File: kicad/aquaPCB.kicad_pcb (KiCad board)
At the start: 2 copper layers, 100 x 100 mm, 149 parts, among them J1 12V IN, J11 SSR G17, J12 SSR G22, J13 SSR G23, J14 SSR G27, J15 IN1, J16 IN2, J17 IN3, J18 IN4, J19 1-Wire 1, J2 Raspberry Pi, J22 I2C 1, J23 I2C 2, J24 Display, J25 pH probe, J26 Module, J27 AIN3, J4 OUT G18, J5 OUT G19, J6 OUT G12, J7 OUT G13, J8 OUT G16, J9 OUT G26, Q1 AOD4184A, Q10 AOD4185, Q2 AOD4184A, Q3 AOD4184A, Q4 AOD4184A, Q5 AOD4184A, Q6 AOD4184A, U1 TPS54360B, U2 AMS1117-3.3, U3 74HCT244D, U4 ULN2803A, U5 ADS1115IDGSR, U6 TLV9062IDR

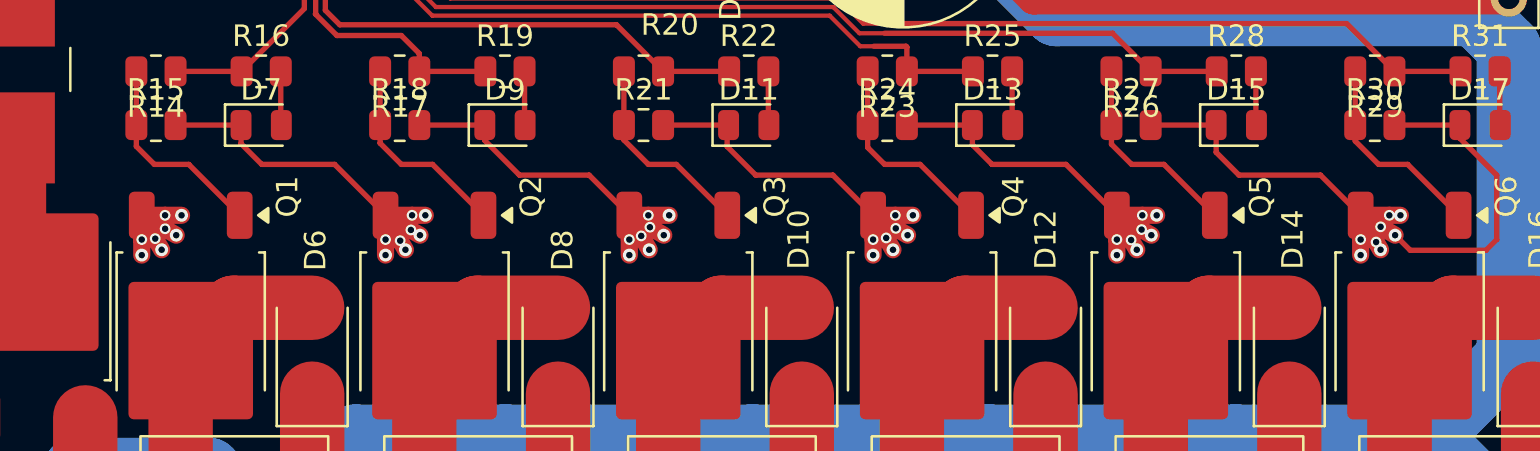
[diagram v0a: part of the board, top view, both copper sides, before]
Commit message: kicad: regular 2x3 source-via blocks with F.Cu GND areas at Q1..Q6
Replaces the 8 crowded vias per MOSFET source (6 hole_to_hole violations)
with 6 vias 0.3/0.6 on a 1 mm grid next to the source pad, joined to the
pad by a small solid F.Cu GND zone (SRC_Qn, priority 2).

Co-Authored-By: Claude Opus 5.5 <noreply@anthropic.com>
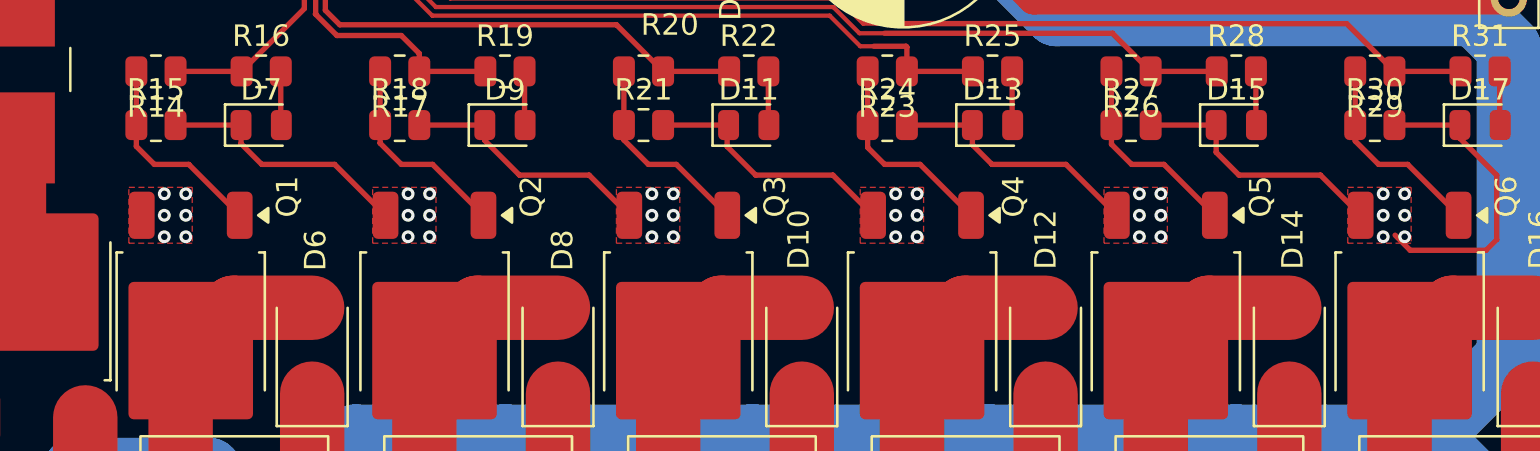
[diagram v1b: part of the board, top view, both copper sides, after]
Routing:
- net GND: track 434.6 -> 390.2 mm, vias 68 -> 56
- added copper zone on F.Cu, net GND

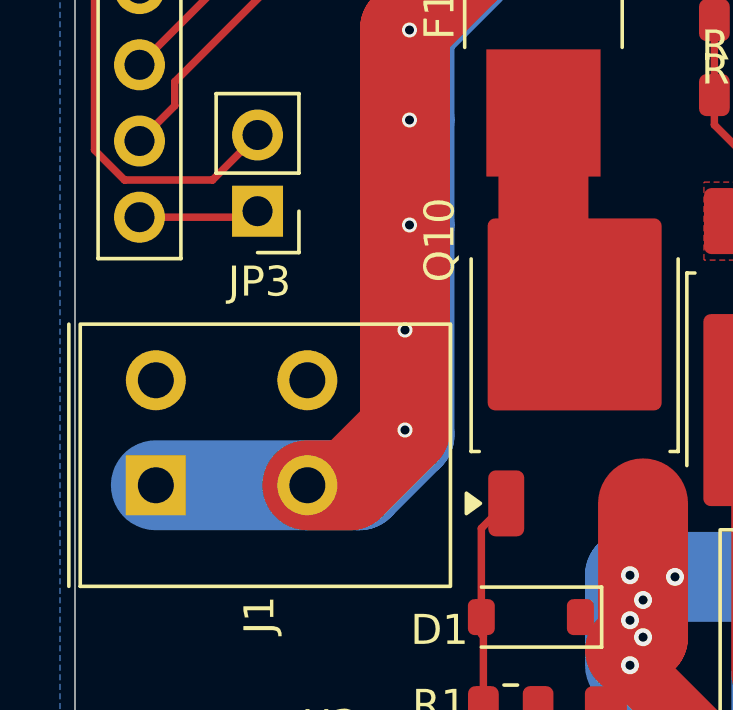
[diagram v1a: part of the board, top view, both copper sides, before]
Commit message: kicad: swap J1 pins (pin 1 = GND), remove floating GND islands
J1 GND now sits on the lower pole, so the ground plane leaves the input
terminal directly east towards Q1..Q6 instead of being boxed in by the
VIN_RAW B.Cu feed. VIN_RAW now starts at the upper pole (3 mm on both
layers as before). Schematic: J1 rotated 180 deg instead of mirrored, wiring
unchanged. GND B.Cu zone island removal set to "always" (removes the
floating 1.05 mm2 island next to J1).

Co-Authored-By: Claude Opus 5.5 <noreply@anthropic.com>
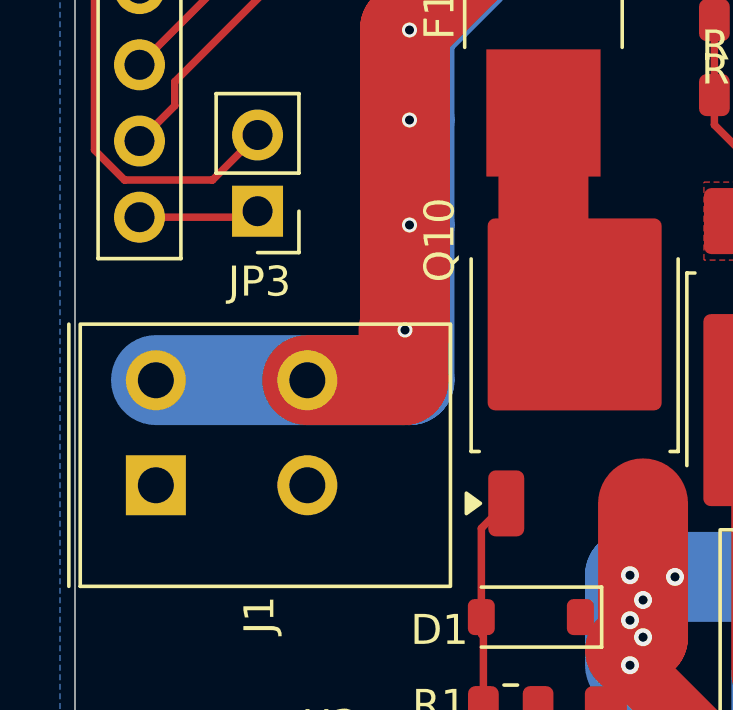
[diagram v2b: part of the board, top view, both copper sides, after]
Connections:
- J1 pad 1: /Power supply/VIN_RAW -> GND
- J1 pad 2: GND -> /Power supply/VIN_RAW
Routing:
- net /Power supply/VIN_RAW: track 49.0 -> 44.0 mm, vias 6 -> 5
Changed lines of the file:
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@@
 			(layers "*.Cu" "*.Mask")
 			(remove_unused_layers no)
-			(net "/Power supply/VIN_RAW")
+			(net "GND")
 			(pinfunction "Pin_1_1")
 			(pintype "passive")
@@
 			(layers "*.Cu" "*.Mask")
 			(remove_unused_layers no)
-			(net "/Power supply/VIN_RAW")
+			(net "GND")
 			(pinfunction "Pin_1_1")
 			(pintype "passive")
@@
 			(layers "*.Cu" "*.Mask")
 			(remove_unused_layers no)
-			(net "GND")
+			(net "/Power supply/VIN_RAW")
 			(pinfunction "Pin_2_2")
 			(pintype "passive")
@@
 			(layers "*.Cu" "*.Mask")
 			(remove_unused_layers no)
-			(net "GND")
+			(net "/Power supply/VIN_RAW")
 			(pinfunction "Pin_2_2")
 			(pintype "passive")
@@
 	)
 	(segment
+		(start 89.8 118.17)
+		(end 89.8 116.5)
+		(width 3)
+		(layer "F.Cu")
+		(net "/Power supply/VIN_RAW")
+	)
+	(segment
 		(start 89.85 116.5)
 		(end 89.85 106.455)
@@
 	)
 	(segment
-		(start 88.009213 121.675)
-		(end 89.85 119.834213)
-		(width 3)
-		(layer "F.Cu")
-		(net "/Power supply/VIN_RAW")
-	)
-	(segment
-		(start 89.85 119.834213)
-		(end 89.85 116.5)
-		(width 3)
-		(layer "F.Cu")
-		(net "/Power supply/VIN_RAW")
-	)
-	(segment
-		(start 86.595 121.675)
-		(end 88.009213 121.675)
+		(start 86.59 118.17)
+		(end 89.8 118.17)
 		(width 3)
 		(layer "F.Cu")
@@
 	)
 	(via
-		(at 89.85 119.834213)
-		(size 0.5)
-		(drill 0.3)
-		(layers "F.Cu" "B.Cu")
-		(net "/Power supply/VIN_RAW")
-	)
-	(via
 		(at 89.85 116.5)
 		(size 0.5)
@@
 	)
 	(segment
-		(start 88.325 121.675)
-		(end 90 120)
-		(width 3)
-		(layer "B.Cu")
-		(net "/Power supply/VIN_RAW")
-	)
-	(segment
 		(start 90 106.5)
 		(end 92 104.5)
@@
 	)
 	(segment
-		(start 81.545 121.675)
-		(end 86.595 121.675)
+		(start 81.55 118.17)
+		(end 86.59 118.17)
 		(width 3)
 		(layer "B.Cu")
@@
 	)
 	(segment
-		(start 90 120)
-		(end 90 113)
+		(start 90 109.5)
+		(end 90 106.5)
 		(width 3)
 		(layer "B.Cu")
@@
 	)
 	(segment
-		(start 90 109.5)
-		(end 90 106.5)
+		(start 86.59 118.17)
+		(end 90 118.17)
 		(width 3)
 		(layer "B.Cu")
@@
 	)
 	(segment
-		(start 86.595 121.675)
-		(end 88.325 121.675)
+		(start 90 118.17)
+		(end 90 113)
 		(width 3)
 		(layer "B.Cu")

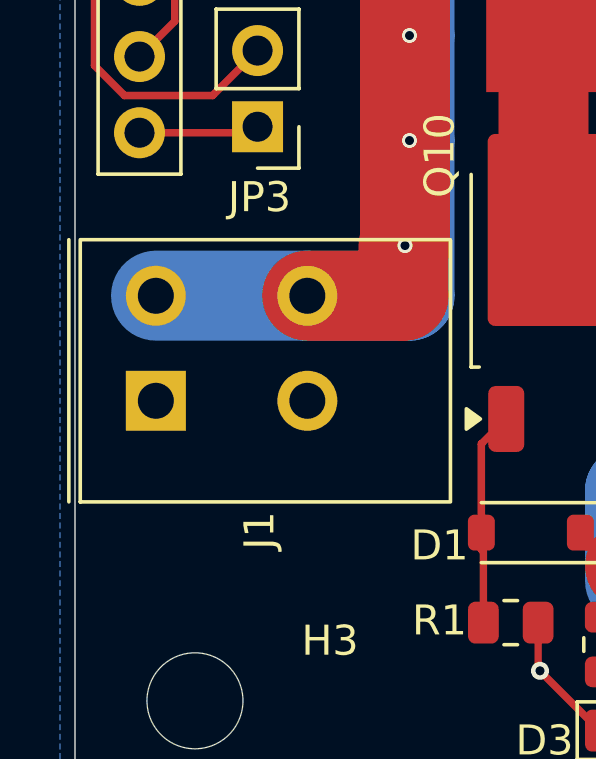
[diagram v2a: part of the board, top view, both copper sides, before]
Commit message: kicad: J1 polarity silk (+12V/GND), connector values match aquaPi port names
Terminal values now use the IoRegistry port names (PWM 0/1, GPIO n,
DS1820, ADC #1 in n) instead of the old "OUT G18"-style labels, several of
which were stale after the 74HCT244 reorder. Values stay on F.Fab; only the
J1 polarity marks are added to the silkscreen.

Co-Authored-By: Claude Opus 5.5 <noreply@anthropic.com>
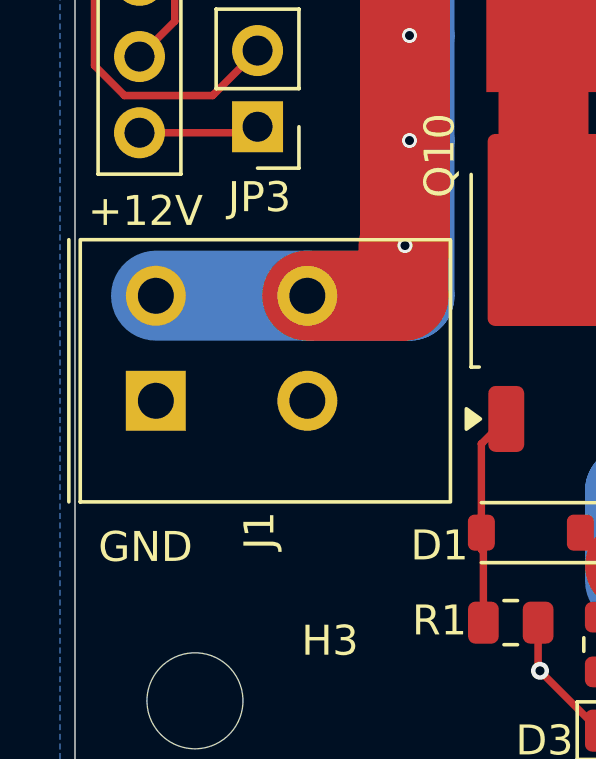
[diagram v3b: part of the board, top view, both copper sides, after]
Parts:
- J11: value SSR G17 -> GPIO 17
- J12: value SSR G22 -> GPIO 22
- J13: value SSR G23 -> GPIO 23
- J14: value SSR G27 -> GPIO 27
- J15: value IN1 -> GPIO 5
- J16: value IN2 -> GPIO 6
- J17: value IN3 -> GPIO 20
- J18: value IN4 -> GPIO 21
- J19: value 1-Wire 1 -> DS1820
- J25: value pH probe -> ADC #1 in 0
- J26: value Module -> ADC #1 in 2
- J27: value AIN3 -> ADC #1 in 3
- J4: value OUT G18 -> PWM 0
- J5: value OUT G19 -> GPIO 12
- J6: value OUT G12 -> GPIO 13
- J7: value OUT G13 -> PWM 1
- J8: value OUT G16 -> GPIO 16
- J9: value OUT G26 -> GPIO 26
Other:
- board text added: "+12V"
- board text added: "GND"
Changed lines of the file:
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@@
 			)
 		)
-		(property "Value" "OUT G16"
+		(property "Value" "GPIO 16"
 			(at 1.275 8.305 180)
 			(layer "F.Fab")
@@
 			)
 		)
-		(property "Value" "SSR G27"
+		(property "Value" "GPIO 27"
 			(at 1 8.305 270)
 			(layer "F.Fab")
@@
 			)
 		)
-		(property "Value" "OUT G12"
+		(property "Value" "GPIO 13"
 			(at 1 8.305 180)
 			(layer "F.Fab")
@@
 			)
 		)
-		(property "Value" "SSR G17"
+		(property "Value" "GPIO 17"
 			(at 1 8.305 270)
 			(layer "F.Fab")
@@
 			)
 		)
-		(property "Value" "IN4"
+		(property "Value" "GPIO 21"
 			(at 2.67 3.3575 0)
 			(layer "F.Fab")
@@
 			)
 		)
-		(property "Value" "OUT G13"
+		(property "Value" "PWM 1"
 			(at 1.424999 8.305 180)
 			(layer "F.Fab")
@@
 			)
 		)
-		(property "Value" "OUT G26"
+		(property "Value" "GPIO 26"
 			(at 1.125 8.305 180)
 			(layer "F.Fab")
@@
 			)
 		)
-		(property "Value" "pH probe"
+		(property "Value" "ADC #1 in 0"
 			(at 0 -14 90)
 			(layer "F.Fab")
@@
 			)
 		)
-		(property "Value" "SSR G23"
+		(property "Value" "GPIO 23"
 			(at 1.155 8.305 270)
 			(layer "F.Fab")
@@
 			)
 		)
-		(property "Value" "1-Wire 1"
+		(property "Value" "DS1820"
 			(at 3.345 8.044999 270)
 			(layer "F.Fab")
@@
 			)
 		)
-		(property "Value" "IN2"
+		(property "Value" "GPIO 6"
 			(at 2.67 3.3575 0)
 			(layer "F.Fab")
@@
 			)
 		)
-		(property "Value" "Module"
+		(property "Value" "ADC #1 in 2"
 			(at 2.67 3.3575 0)
 			(layer "F.Fab")
@@
 			)
 		)
-		(property "Value" "OUT G19"
+		(property "Value" "GPIO 12"
 			(at 1 8.305 180)
 			(layer "F.Fab")
@@
 			)
 		)
-		(property "Value" "IN1"
+		(property "Value" "GPIO 5"
 			(at 2.67 3.3575 0)
 			(layer "F.Fab")
@@
 			)
 		)
-		(property "Value" "SSR G22"
+		(property "Value" "GPIO 22"
 			(at 1 8.305 270)
 			(layer "F.Fab")
@@
 			)
 		)
-		(property "Value" "IN3"
+		(property "Value" "GPIO 20"
 			(at 2.67 3.3575 0)
 			(layer "F.Fab")
@@
 			)
 		)
-		(property "Value" "OUT G18"
+		(property "Value" "PWM 0"
 			(at 1 8.305 180)
 			(layer "F.Fab")
@@
 			)
 		)
-		(property "Value" "AIN3"
+		(property "Value" "ADC #1 in 3"
 			(at 2.67 2.045 90)
 			(layer "F.Fab")
@@
 		(layer "Edge.Cuts")
 	)
+	(gr_text "+12V"
+		(at 81.2 115.35 0)
+		(layer "F.SilkS")
+		(effects
+			(font
+				(size 1 1)
+				(thickness 0.16)
+			)
+		)
+	)
+	(gr_text "GND"
+		(at 81.2 126.55 0)
+		(layer "F.SilkS")
+		(effects
+			(font
+				(size 1 1)
+				(thickness 0.16)
+			)
+		)
+	)
 	(segment
